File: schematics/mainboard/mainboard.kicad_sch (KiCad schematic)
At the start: 82 parts, among them J1 ICSP, J10 Conn_AGauge, J11 Conn_SAS, J2 USB_B_Micro, J3 DEALON DC-S050-200, J4 PWR_SELECT, J5 Conn_Joy1, J6 Conn_Joy2, J7 Conn_Throttle, J8 Conn_DGauges, J9 Conn_LCD, Q2 BC849, U1 ATmega2560-16A, U2 FT232RL, U3 USBLC6-2P6, U4 AIP78M05, U5 L9110, U6 74HC595, U7 74HC595, U8 74HC165, U9 74HC165, Y1 16Mhz

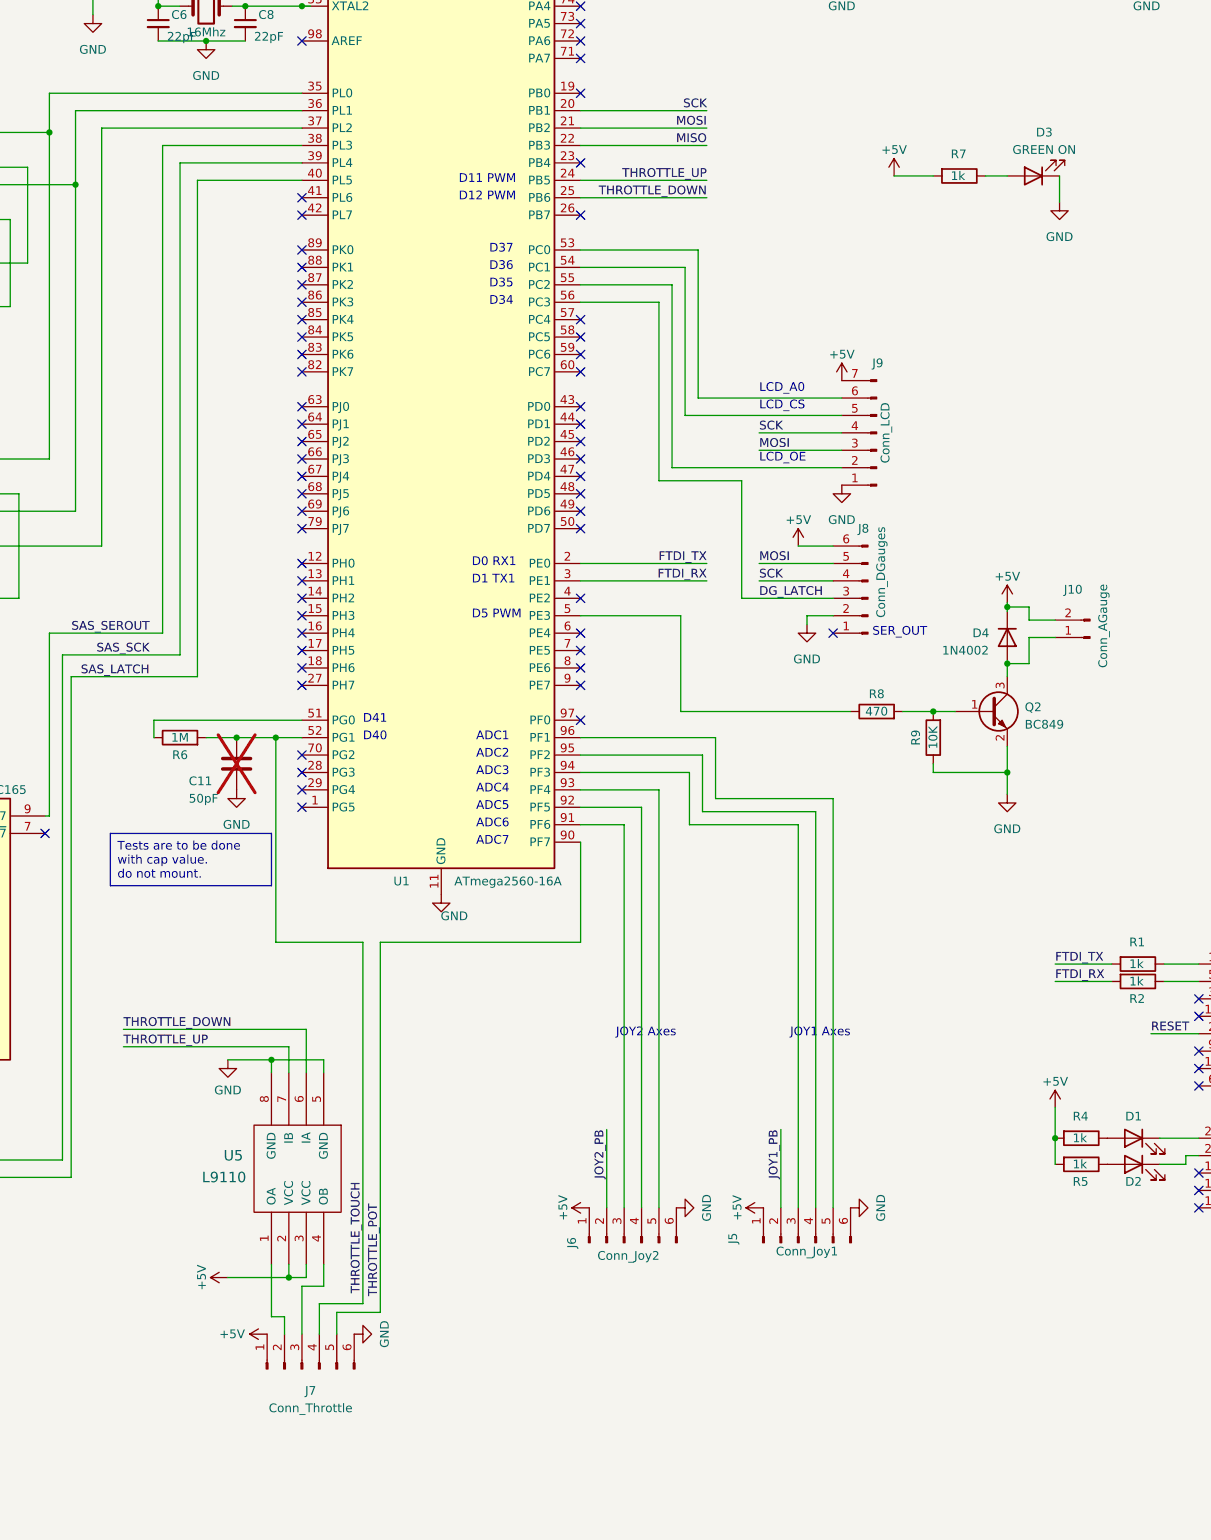
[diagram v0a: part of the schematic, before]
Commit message: SCH:MB=> add pull-up to throttle signals
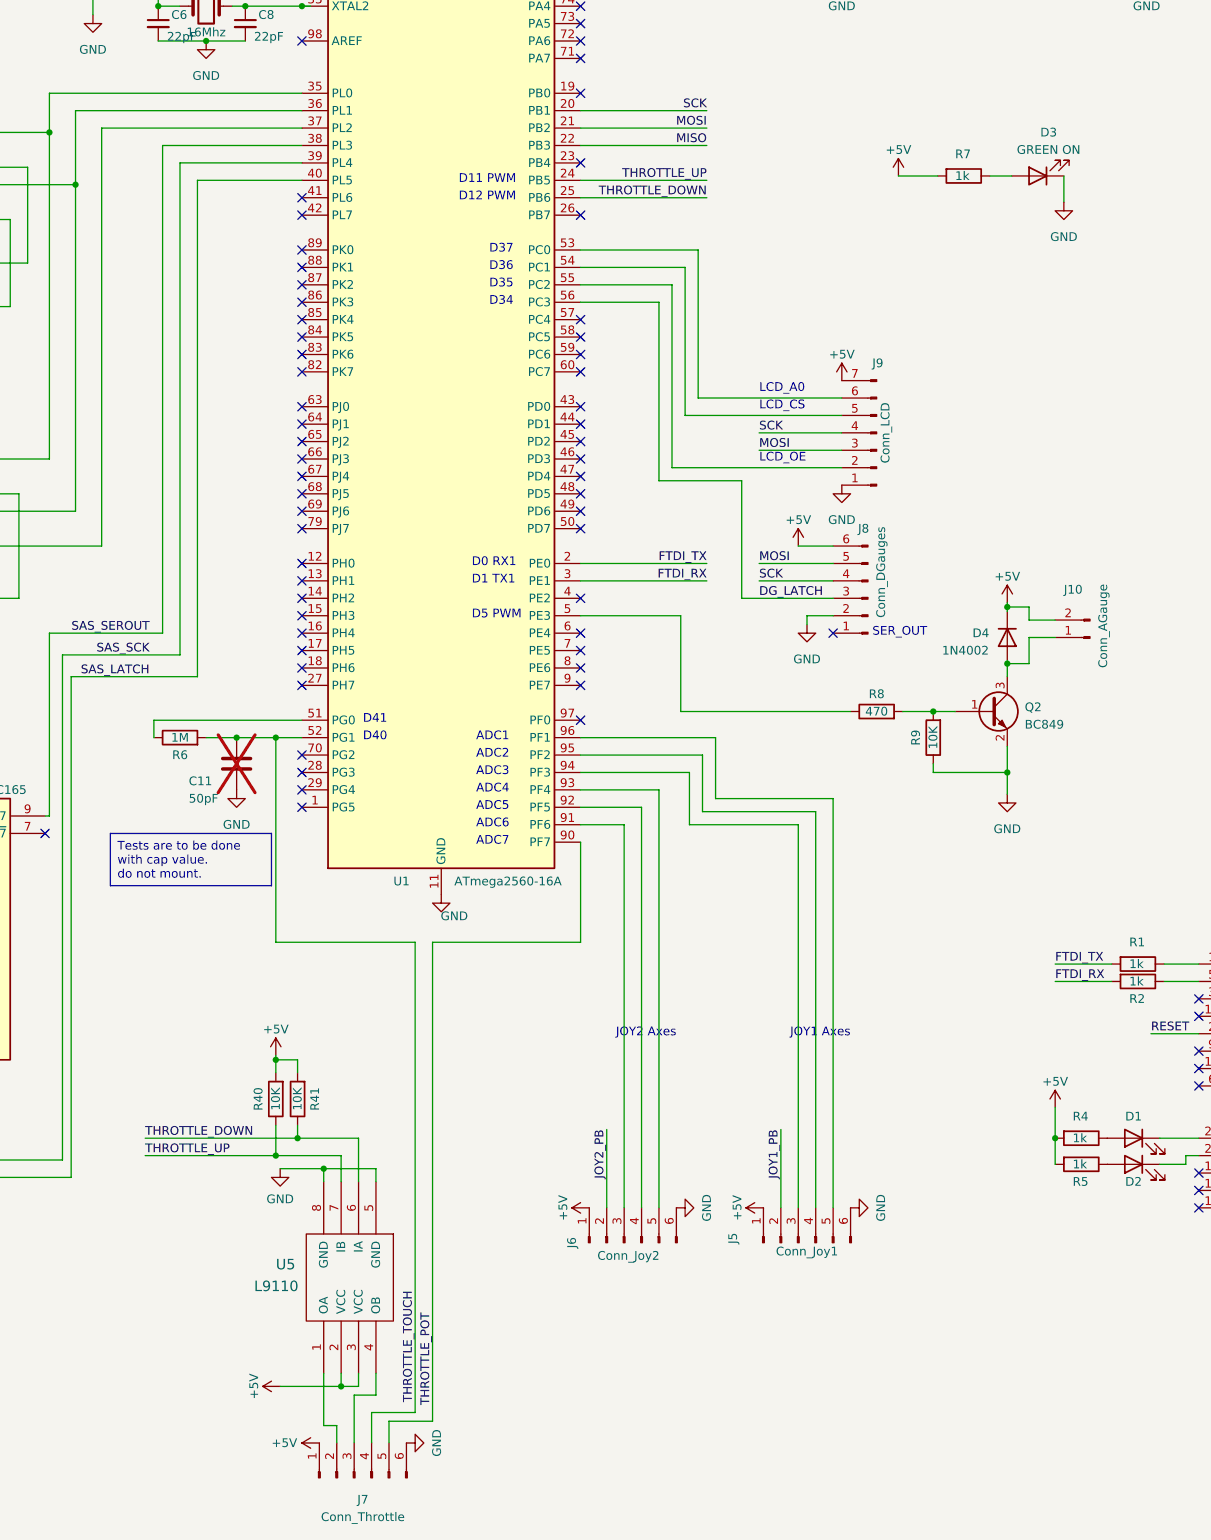
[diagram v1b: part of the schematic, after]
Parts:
- added R40, R41: 10K, Resistor_SMD:R_0603_1608Metric, symbol Device:R
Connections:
- net +5V: now also R40.2, R41.2
- net THROTTLE_DOWN: now also R41.1
- net THROTTLE_UP: now also R40.1
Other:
- moved on the sheet: D3, J7, R7, U5

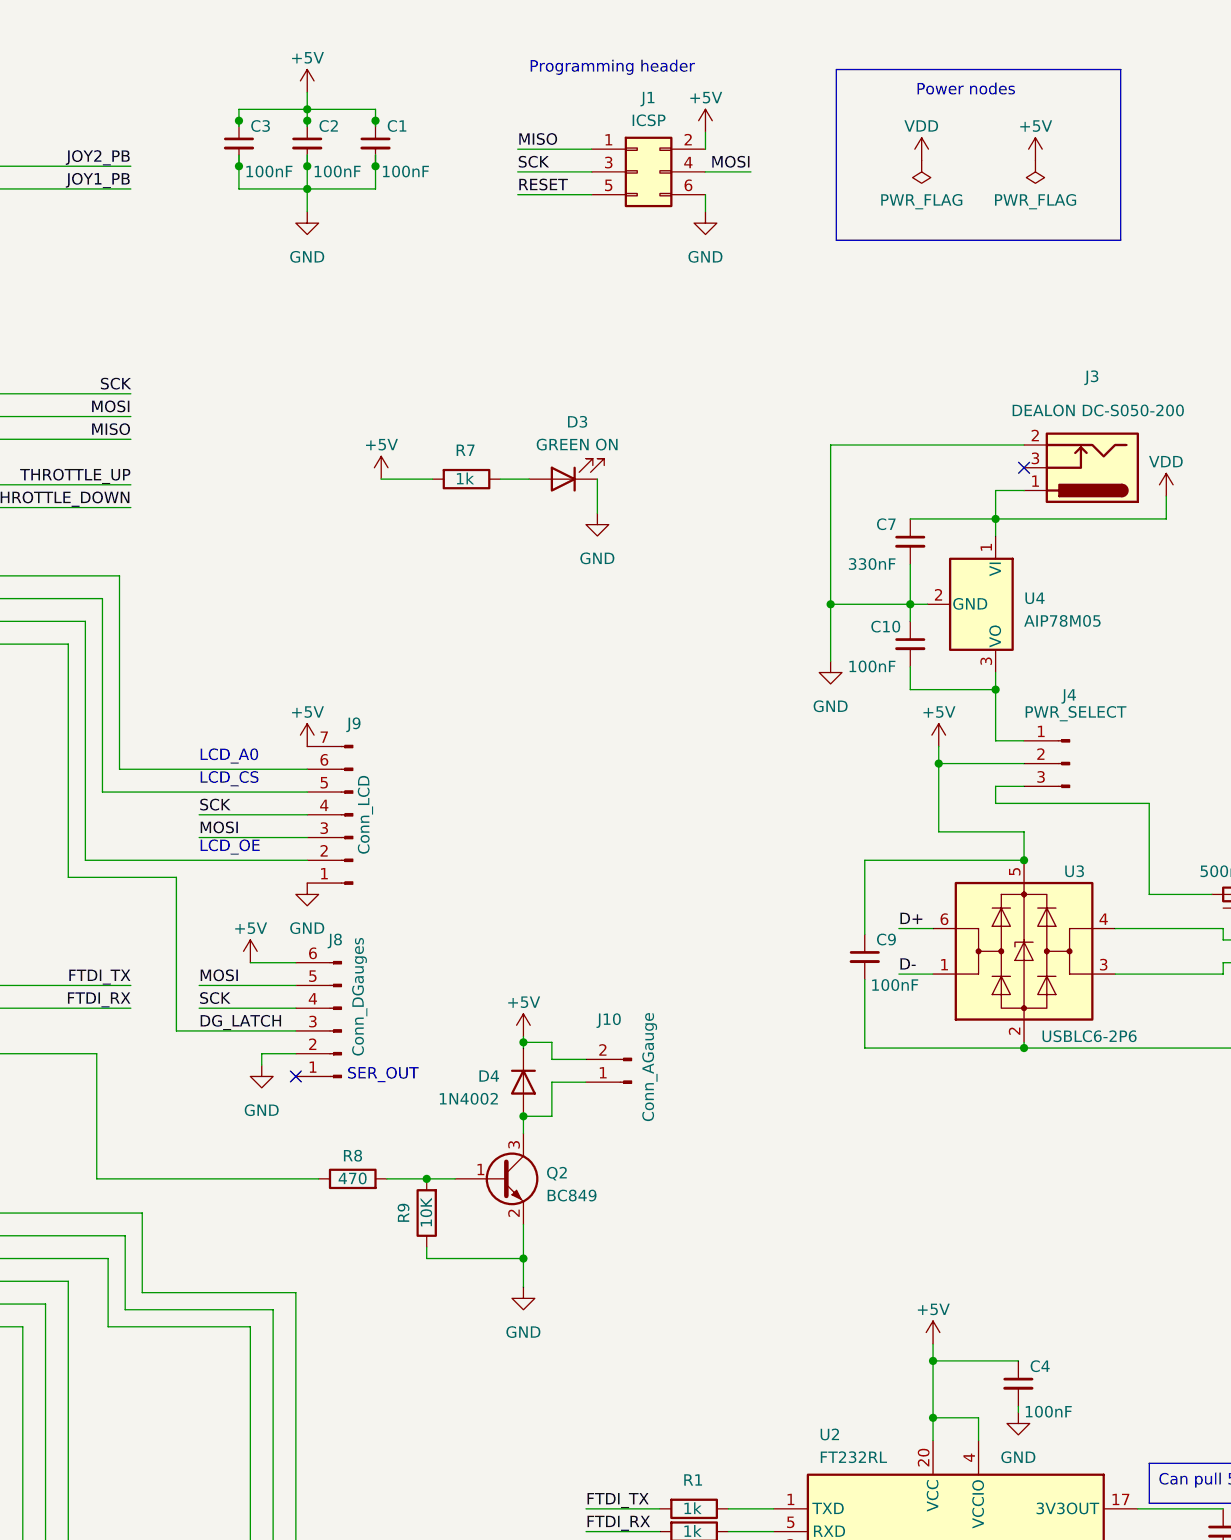
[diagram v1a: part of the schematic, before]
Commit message: SCH:MB=> moved decoupling caps to each +5V on the ATMega
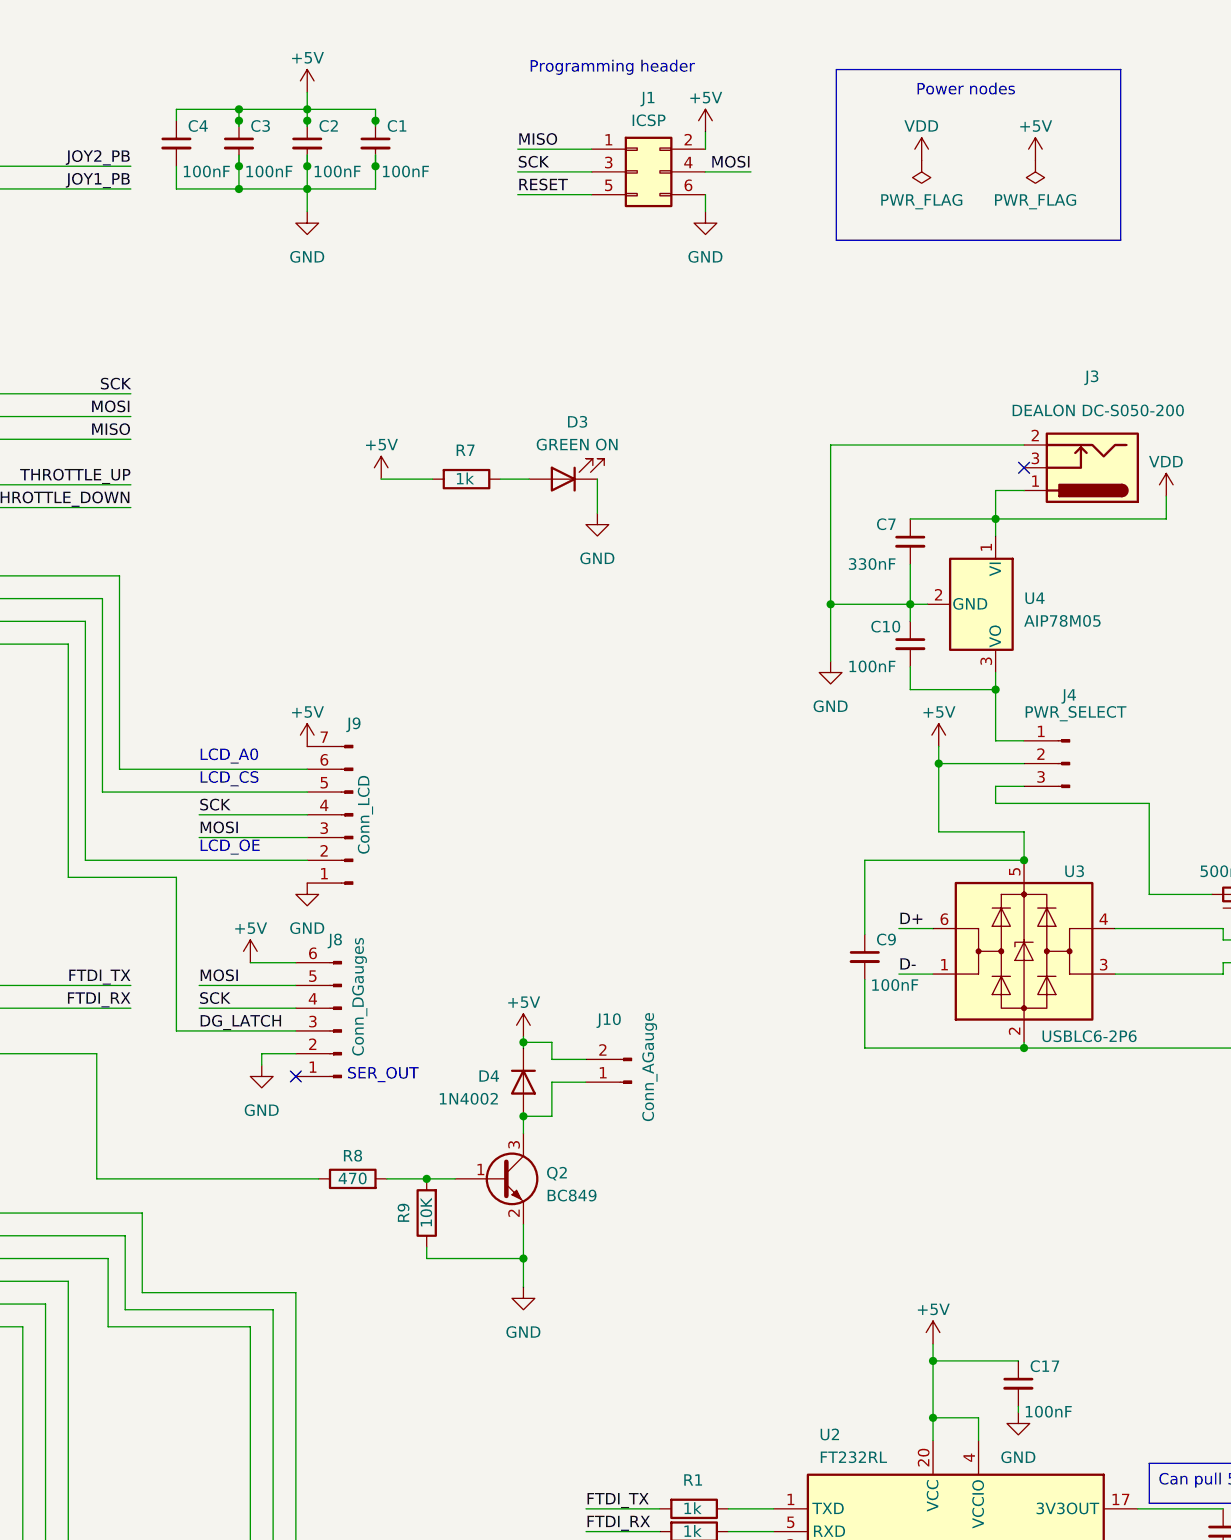
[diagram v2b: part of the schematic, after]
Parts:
- added C4: 100nF, Capacitor_SMD:C_0603_1608Metric, symbol Device:C_Small
- renumbered C4 to C17
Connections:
- net +5V: now also C4.1
- net GND: now also C4.2
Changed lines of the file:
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@@
   (junction (at 181.61 254) (diameter 0) (color 0 0 0 0)
   )
+  (junction (at 320.675 99.06) (diameter 0) (color 0 0 0 0)
+  )
   (junction (at 171.45 243.84) (diameter 0) (color 0 0 0 0)
   )
@@
   (junction (at 107.315 246.38) (diameter 0) (color 0 0 0 0)
   )
+  (junction (at 320.675 107.95) (diameter 0) (color 0 0 0 0)
+  )
   (junction (at 408.305 203.835) (diameter 0) (color 0 0 0 0)
   )
@@
     (stroke (width 0) (type default))
   )
-  (wire (pts (xy 320.675 99.06) (xy 328.295 99.06))
-    (stroke (width 0) (type default))
-  )
   (wire (pts (xy 355.6 207.645) (xy 355.6 211.455))
     (stroke (width 0) (type default))
@@
     (stroke (width 0) (type default))
   )
+  (wire (pts (xy 313.69 99.06) (xy 313.69 100.33))
+    (stroke (width 0) (type default))
+  )
   (wire (pts (xy 112.395 251.46) (xy 112.395 266.7))
     (stroke (width 0) (type default))
@@
     (stroke (width 0) (type default))
   )
+  (wire (pts (xy 313.69 105.41) (xy 313.69 107.95))
+    (stroke (width 0) (type default))
+  )
+  (wire (pts (xy 320.675 99.06) (xy 328.295 99.06))
+    (stroke (width 0) (type default))
+  )
   (wire (pts (xy 395.605 161.29) (xy 395.605 163.83))
     (stroke (width 0) (type default))
@@
     (stroke (width 0) (type default))
   )
+  (wire (pts (xy 313.69 99.06) (xy 320.675 99.06))
+    (stroke (width 0) (type default))
+  )
   (bus (pts (xy 81.28 269.24) (xy 94.615 269.24))
     (stroke (width 0) (type default))
@@
     (stroke (width 0) (type default))
   )
+  (wire (pts (xy 313.69 107.95) (xy 320.675 107.95))
+    (stroke (width 0) (type default))
+  )
   (wire (pts (xy 341.63 218.44) (xy 344.805 218.44))
     (stroke (width 0) (type default))
@@
     (stroke (width 0) (type default))
   )
+  (wire (pts (xy 320.675 107.95) (xy 328.295 107.95))
+    (stroke (width 0) (type default))
+  )
   (wire (pts (xy 96.52 238.76) (xy 99.695 238.76))
     (stroke (width 0) (type default))
@@
     (stroke (width 0) (type default))
   )
-  (wire (pts (xy 320.675 107.95) (xy 328.295 107.95))
-    (stroke (width 0) (type default))
-  )
   (wire (pts (xy 290.195 234.95) (xy 296.545 234.95))
     (stroke (width 0) (type default))
@@
   (symbol (lib_id "Device:C_Small") (at 407.67 241.3 0) (unit 1)
     (in_bom yes) (on_board yes) (dnp no)
-    (property "Reference" "C4" (at 408.94 239.395 0)
+    (property "Reference" "C17" (at 408.94 239.395 0)
       (effects (font (size 1.27 1.27)) (justify left))
     )
@@
       (project "mainboard"
         (path "/d7de281c-a164-4408-aff7-47d87383fb97"
-          (reference "C4") (unit 1)
+          (reference "C17") (unit 1)
         )
       )
@@
         )
       )
+    )
+  )
+  (symbol (lib_id "Device:C_Small") (at 313.69 102.87 0) (unit 1)
+    (in_bom yes) (on_board yes) (dnp no)
+    (property "Reference" "C4" (at 314.96 100.965 0)
+      (effects (font (size 1.27 1.27)) (justify left))
+    )
+    (property "Value" "100nF" (at 314.325 106.045 0)
+      (effects (font (size 1.27 1.27)) (justify left))
+    )
+    (property "Footprint" "Capacitor_SMD:C_0603_1608Metric" (at 313.69 102.87 0)
+      (effects (font (size 1.27 1.27)) hide)
+    )
+    (property "Datasheet" "~" (at 313.69 102.87 0)
+      (effects (font (size 1.27 1.27)) hide)
+    )
+    (property "lcsc" "C30926" (at 313.69 102.87 0)
+      (effects (font (size 1.27 1.27)) hide)
+    )
+    (pin "1")
+    (pin "2")
+    (instances
+      (project "mainboard"
+        (path "/d7de281c-a164-4408-aff7-47d87383fb97"
+          (reference "C4") (unit 1)
+        )
+      )
